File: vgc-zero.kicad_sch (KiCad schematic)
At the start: 22 parts, among them J1 Conn_01x05_Pin, J2 Conn_01x05_Pin, J3 Conn_01x05_Pin, J4 Conn_01x02_Pin, SW1 SW_Push, SW10 SW_Push, SW11 SW_SPDT, SW2 SW_Push, SW3 SW_Push, SW4 SW_Push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

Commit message: move symbols to project library
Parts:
- CHARGER1: symbol vgc:TP4056_CHARGER -> vgc-zero-symbols:TP4056_CHARGER
- DISP1: symbol vgc:SSD1351_OLED_128x128 -> vgc-zero-symbols:SSD1351_OLED_128x128
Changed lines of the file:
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@@
 	)
 	(symbol
-		(lib_id "vgc:TP4056_CHARGER")
+		(lib_id "vgc-zero-symbols:TP4056_CHARGER")
 		(at 226.06 93.98 180)
 		(unit 1)
@@
 	)
 	(symbol
-		(lib_id "vgc:SSD1351_OLED_128x128")
+		(lib_id "vgc-zero-symbols:SSD1351_OLED_128x128")
 		(at 203.2 57.15 90)
 		(mirror x)

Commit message: pcb done
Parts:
- removed J4: Conn_01x02_Pin, Connector_PinHeader_1.00mm:PinHeader_1x02_P1.00mm_Horizontal, symbol Connector:Conn_01x02_Pin
- added H1: MountingHole_Pad, MountingHole:MountingHole_3.2mm_M3_Pad, symbol Mechanical:MountingHole_Pad
- D1: footprint LED_THT:LED_D3.0mm -> LED_SMD:LED_1210_3225Metric_Pad1.42x2.65mm_HandSolder
- J1, J2, J3: value Conn_01x05_Pin -> Conn_01x06_Pin; footprint Connector_PinHeader_1.00mm:PinHeader_1x05_P1.00mm_Horizontal -> Connector_PinHeader_2.54mm:PinHeader_1x06_P2.54mm_Horizontal; symbol Connector:Conn_01x05_Pin -> Connector:Conn_01x06_Pin
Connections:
- net 3V3: now also J1.6 (Pin_6), J2.6 (Pin_6), J3.6 (Pin_6)
- net GND: now also H1.1

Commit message: update to 1.1.0
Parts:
- removed BT1: LIPO-BATTERY, Connector_JST:JST_PH_S2B-PH-K_1x02_P2.00mm_Horizontal, symbol Device:Battery_Cell
- removed CHARGER1: TP4056_CHARGER, vgc-zero-footprints:Tp4056_Charger, symbol vgc-zero-symbols:TP4056_CHARGER
- added H2, H3, H4, H5, H6: MountingHole_Pad, MountingHole:MountingHole_2.2mm_M2_Pad, symbol Mechanical:MountingHole_Pad
- DISP1: footprint vgc-zero-footprints:SSD1351_OLED_128x128 -> Connector_JST:JST_PH_S7B-PH-K_1x07_P2.00mm_Horizontal
- H1: footprint MountingHole:MountingHole_3.2mm_M3_Pad -> MountingHole:MountingHole_2.2mm_M2_Pad
- LS1: footprint Connector_Wire:SolderWire-0.1sqmm_1x02_P3.6mm_D0.4mm_OD1mm -> Buzzer_Beeper:Buzzer_12x9.5RM7.6
- MCU1: footprint Module:RaspberryPi_Pico_SMD_HandSolder -> Module:RaspberryPi_Pico_Common_THT; symbol MCU_Module:RaspberryPi_Pico_Debug -> MCU_Module:RaspberryPi_Pico
- SW1, SW10, SW2, SW3, SW4, SW5, SW6, SW7, SW8, SW9: footprint vgc-zero-footprints:SW_PUSH_RUBBER_8mm -> Button_Switch_THT:SW_PUSH_6mm_H5mm
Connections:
- net 3V3: now also SW11.3 (C)
- net GND: now also SW11.1 (A), H2.1, H3.1, H4.1, H5.1, H6.1; no longer MCU1.D2 (GND)
- net at SW11.2 (B): now also J2.3 (Pin_3), MCU1.37 (3V3_EN)
- net VCC: no longer names the net of MCU1.39 (VSYS)
- net VCC: no longer SW11.1 (A)
- no-connect marks 6 -> 2
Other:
- moved on the sheet: DISP1, SW11

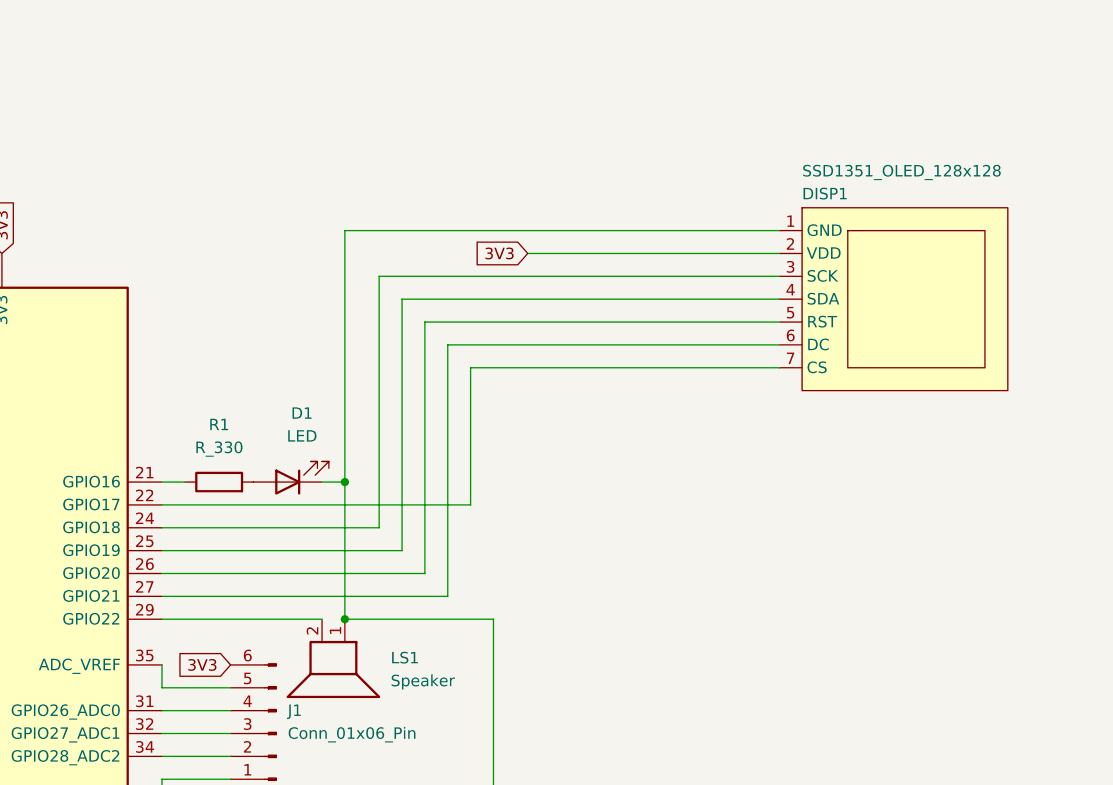
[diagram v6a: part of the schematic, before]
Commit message: adjust display pins
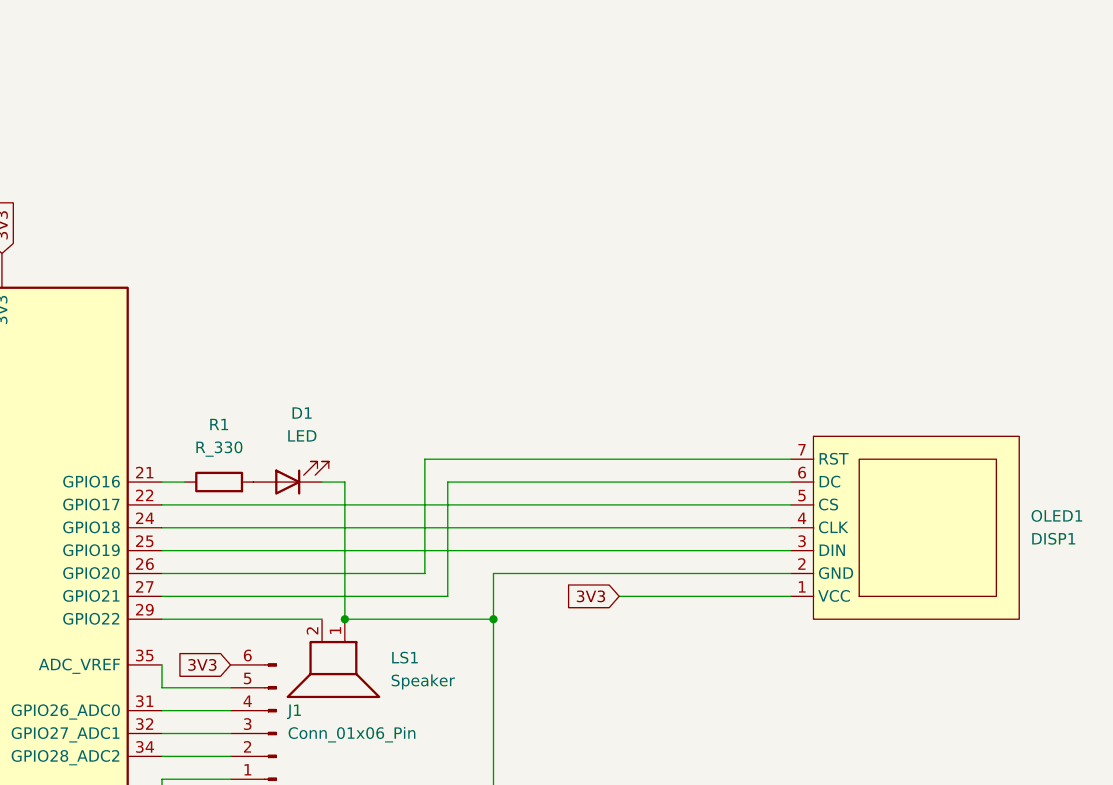
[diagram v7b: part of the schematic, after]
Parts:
- removed DISP1: SSD1351_OLED_128x128, Connector_JST:JST_PH_S7B-PH-K_1x07_P2.00mm_Horizontal, symbol vgc-zero-symbols:SSD1351_OLED_128x128
- added OLED1: DISP1, Connector_JST:JST_PH_S7B-PH-K_1x07_P2.00mm_Horizontal, symbol vgc-zero-symbols:SSD1351_OLED_128x128_WAVESHARE
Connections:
- net 3V3: now also OLED1.1 (VCC)
- net GND: now also OLED1.2 (GND)
- net at MCU1.22 (GPIO17): now also OLED1.5 (CS)
- net at MCU1.24 (GPIO18): now also OLED1.4 (CLK)
- net at MCU1.25 (GPIO19): now also OLED1.3 (DIN)
- net at MCU1.26 (GPIO20): now also OLED1.7 (RST)
- net at MCU1.27 (GPIO21): now also OLED1.6 (DC)
